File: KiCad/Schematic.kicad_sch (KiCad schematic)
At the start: 44 parts, among them U4 LMH6609MF, U5 LMH6609MF, U6 LMH6609MF, U7 LMH6609MF, U8 LMH6609MF, U9 LMH6609MF

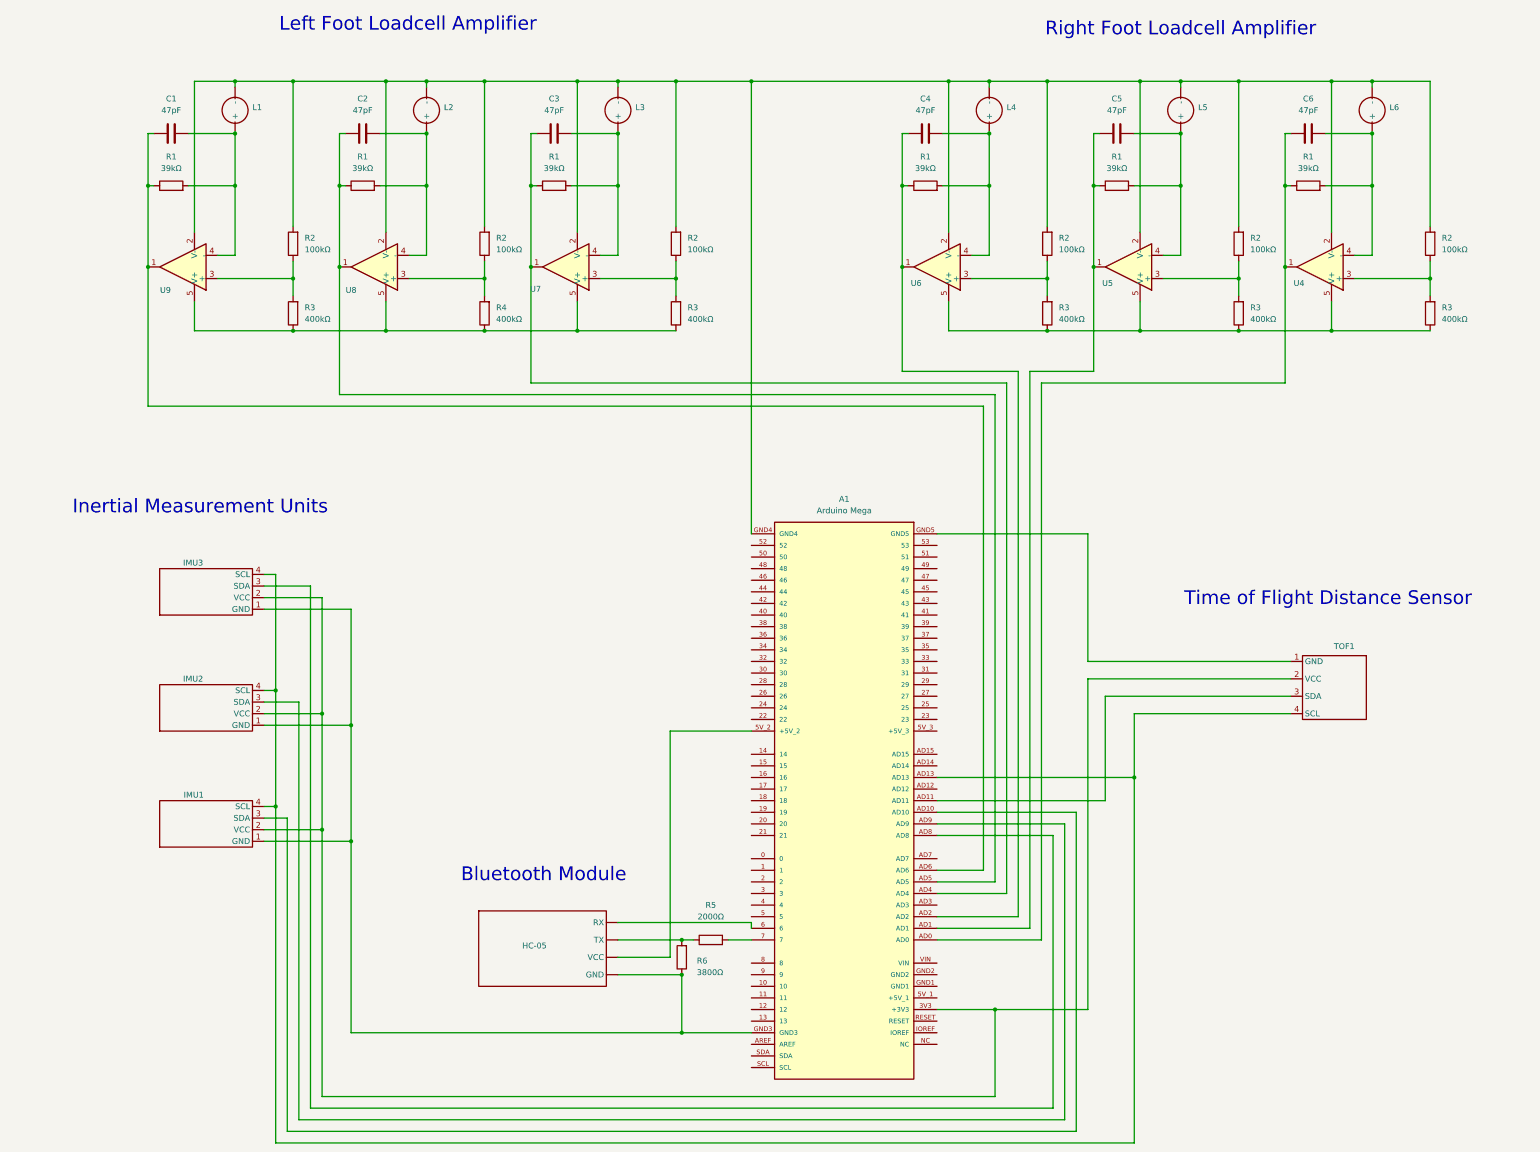
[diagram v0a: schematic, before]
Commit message: Changed wires and Component background color
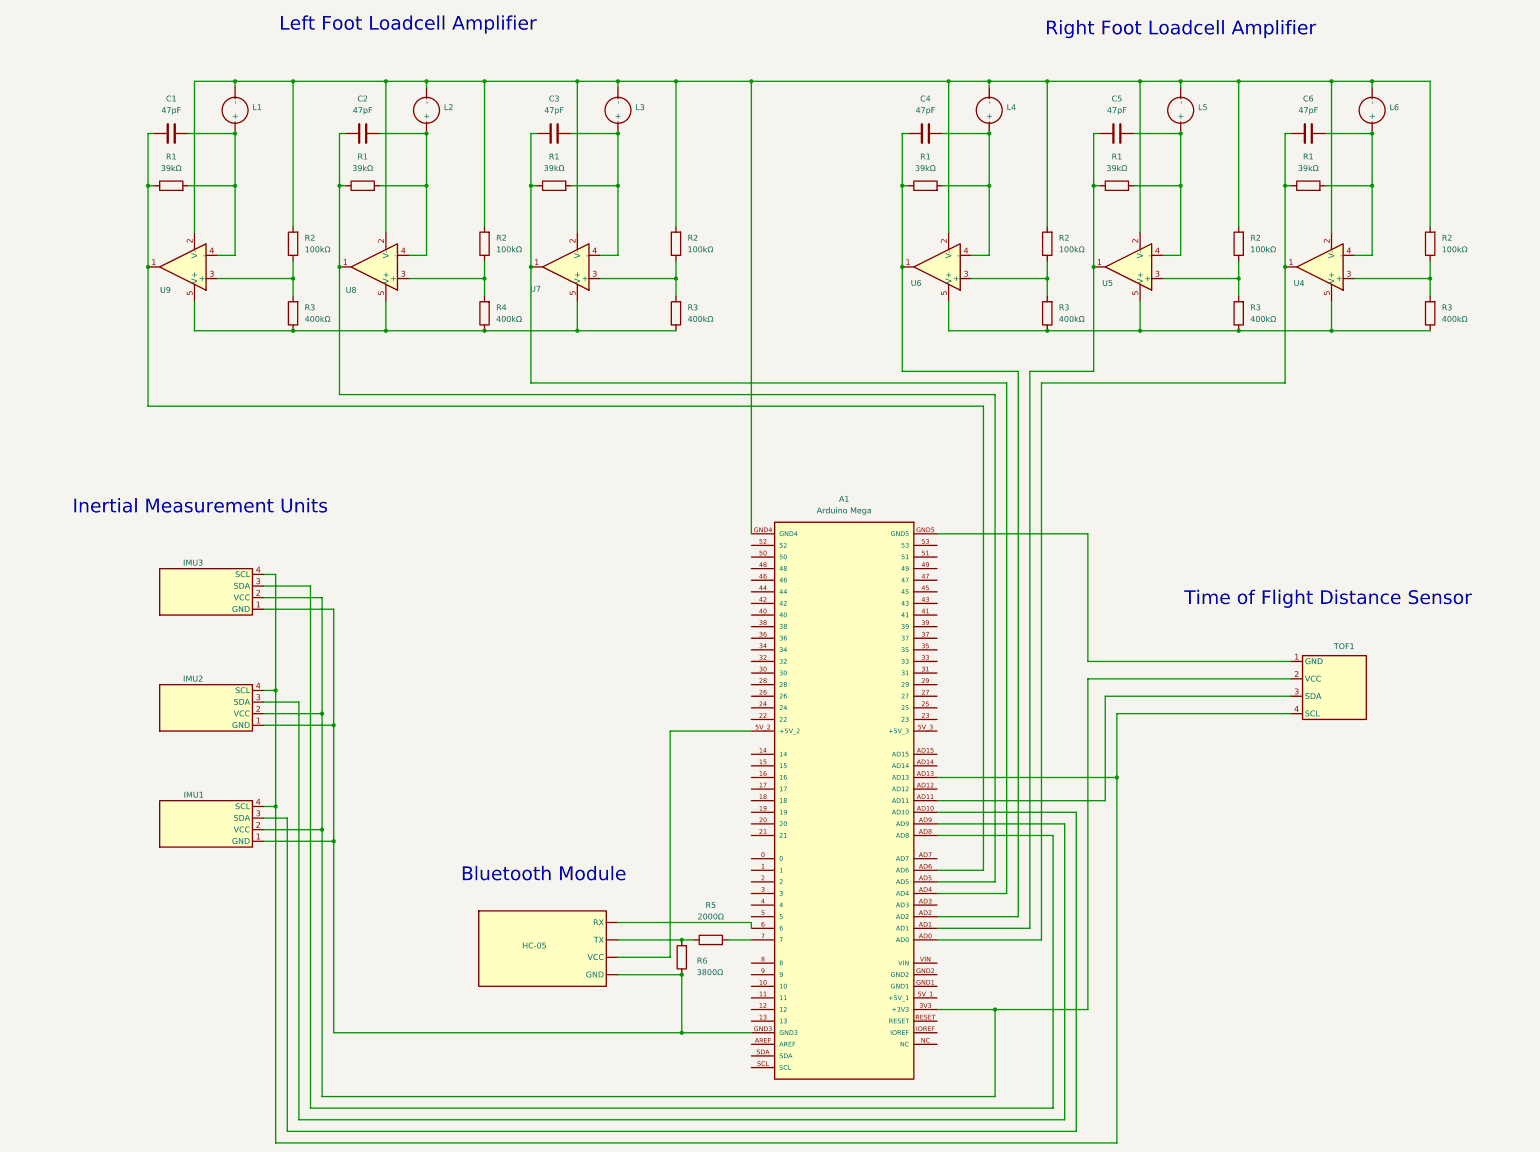
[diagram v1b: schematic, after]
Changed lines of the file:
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@@
 	)
 	(junction
-		(at 113.03 179.07)
-		(diameter 0)
-		(color 0 0 0 0)
-	)
-	(junction
 		(at 185.42 226.06)
 		(diameter 0)
@@
 	)
 	(junction
+		(at 280.67 190.5)
+		(diameter 0)
+		(color 0 0 0 0)
+	)
+	(junction
 		(at 285.75 92.71)
 		(diameter 0)
@@
 	)
 	(junction
-		(at 284.48 190.5)
-		(diameter 0)
-		(color 0 0 0 0)
-	)
-	(junction
 		(at 184.15 81.28)
 		(diameter 0)
@@
 	)
 	(junction
-		(at 113.03 204.47)
-		(diameter 0)
-		(color 0 0 0 0)
-	)
-	(junction
 		(at 120.65 38.1)
 		(diameter 0)
@@
 	)
 	(junction
+		(at 109.22 179.07)
+		(diameter 0)
+		(color 0 0 0 0)
+	)
+	(junction
+		(at 109.22 204.47)
+		(diameter 0)
+		(color 0 0 0 0)
+	)
+	(junction
 		(at 68.58 78.74)
 		(diameter 0)
@@
 	(wire
 		(pts
-			(xy 284.48 176.53) (xy 318.77 176.53)
+			(xy 280.67 176.53) (xy 318.77 176.53)
 		)
 		(stroke
@@
 	(wire
 		(pts
-			(xy 113.03 204.47) (xy 113.03 246.38)
+			(xy 109.22 204.47) (xy 109.22 246.38)
 		)
 		(stroke
@@
 	(wire
 		(pts
-			(xy 96.52 270.51) (xy 284.48 270.51)
+			(xy 96.52 270.51) (xy 280.67 270.51)
 		)
 		(stroke
@@
 	(wire
 		(pts
-			(xy 284.48 190.5) (xy 284.48 176.53)
+			(xy 280.67 190.5) (xy 280.67 176.53)
 		)
 		(stroke
@@
 	(wire
 		(pts
-			(xy 113.03 153.67) (xy 113.03 179.07)
+			(xy 109.22 153.67) (xy 109.22 179.07)
 		)
 		(stroke
@@
 	(wire
 		(pts
-			(xy 93.98 153.67) (xy 113.03 153.67)
+			(xy 93.98 153.67) (xy 109.22 153.67)
 		)
 		(stroke
@@
 	(wire
 		(pts
-			(xy 241.3 190.5) (xy 284.48 190.5)
+			(xy 241.3 190.5) (xy 280.67 190.5)
 		)
 		(stroke
@@
 	(wire
 		(pts
-			(xy 284.48 270.51) (xy 284.48 190.5)
+			(xy 280.67 270.51) (xy 280.67 190.5)
 		)
 		(stroke
@@
 	(wire
 		(pts
-			(xy 113.03 246.38) (xy 185.42 246.38)
+			(xy 109.22 246.38) (xy 185.42 246.38)
 		)
 		(stroke
@@
 	(wire
 		(pts
-			(xy 93.98 204.47) (xy 113.03 204.47)
+			(xy 93.98 204.47) (xy 109.22 204.47)
 		)
 		(stroke
@@
 	(wire
 		(pts
-			(xy 93.98 179.07) (xy 113.03 179.07)
+			(xy 93.98 179.07) (xy 109.22 179.07)
 		)
 		(stroke
@@
 	(wire
 		(pts
-			(xy 113.03 179.07) (xy 113.03 204.47)
+			(xy 109.22 179.07) (xy 109.22 204.47)
 		)
 		(stroke
@@
 	)
 	(symbol
-		(lib_name "Bluetooth_Module_HC-05_1")
 		(lib_id "ProjectSymbols:Bluetooth_Module_HC-05")
 		(at 153.67 228.6 90)

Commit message: Update Schematic.kicad_sch
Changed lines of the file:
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@@
-	)
-	(junction
-		(at 280.67 190.5)
-		(diameter 0)
-		(color 0 0 0 0)
 	)
 	(junction
@@
 	)
 	(junction
+		(at 279.4 190.5)
+		(diameter 0)
+		(color 0 0 0 0)
+	)
+	(junction
 		(at 120.65 92.71)
 		(diameter 0)
@@
 	(wire
 		(pts
-			(xy 280.67 176.53) (xy 318.77 176.53)
+			(xy 279.4 176.53) (xy 318.77 176.53)
 		)
 		(stroke
@@
 	(wire
 		(pts
-			(xy 318.77 172.72) (xy 278.13 172.72)
-		)
-		(stroke
-			(width 0)
-			(type default)
-		)
-	)
-	(wire
-		(pts
-			(xy 96.52 270.51) (xy 280.67 270.51)
+			(xy 318.77 172.72) (xy 276.86 172.72)
+		)
+		(stroke
+			(width 0)
+			(type default)
+		)
+	)
+	(wire
+		(pts
+			(xy 96.52 270.51) (xy 279.4 270.51)
 		)
 		(stroke
@@
 	(wire
 		(pts
-			(xy 280.67 190.5) (xy 280.67 176.53)
+			(xy 279.4 190.5) (xy 279.4 176.53)
 		)
 		(stroke
@@
 	(wire
 		(pts
-			(xy 278.13 195.58) (xy 241.3 195.58)
+			(xy 276.86 195.58) (xy 241.3 195.58)
 		)
 		(stroke
@@
 	(wire
 		(pts
-			(xy 241.3 190.5) (xy 280.67 190.5)
+			(xy 241.3 190.5) (xy 279.4 190.5)
 		)
 		(stroke
@@
 	(wire
 		(pts
-			(xy 278.13 172.72) (xy 278.13 195.58)
-		)
-		(stroke
-			(width 0)
-			(type default)
-		)
-	)
-	(wire
-		(pts
-			(xy 280.67 270.51) (xy 280.67 190.5)
-		)
-		(stroke
+			(xy 276.86 172.72) (xy 276.86 195.58)
+		)
+		(stroke
+			(width 0)
+			(type default)
+		)
+	)
+	(wire
+		(pts
+			(xy 279.4 270.51) (xy 279.4 190.5)
+		)
+		(stroke

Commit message: Added Arduino mega label
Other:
- note added: "Arduino Mega"
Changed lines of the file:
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@@
+		)
+	)
+	(text "Arduino Mega"
+		(exclude_from_sim no)
+		(at 219.964 122.682 0)
+		(effects
+			(font
+				(size 3 3)
+			)
 		)
 	)

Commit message: Schematic update
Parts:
- renumbered IMU3 to IMU1, IMU1 to IMU3, R6 to R10, R5 to R11, R1 to R12, R2 to R13, R3 to R14, R1 to R15, R2 to R16, R3 to R17, R1 to R18, R2 to R19, R3 to R20, R1 to R4, R2 to R5, R4 to R6, R1 to R7, R2 to R8, R3 to R9, U9 to U1, U8 to U2, U7 to U3, U6 to U4, U4 to U6
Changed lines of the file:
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@@
 			(font
 				(size 3 3)
+				(thickness 0.6)
+				(bold yes)
 			)
 		)
@@
 	(text "Arduino Mega"
 		(exclude_from_sim no)
-		(at 219.964 122.682 0)
+		(at 220.472 126.746 0)
 		(effects
 			(font
 				(size 3 3)
+				(thickness 0.6)
+				(bold yes)
 			)
 		)
@@
 	(text "Bluetooth Module"
 		(exclude_from_sim no)
-		(at 155.194 211.836 0)
+		(at 156.464 213.36 0)
 		(effects
 			(font
 				(size 3 3)
+				(thickness 0.6)
+				(bold yes)
 			)
 		)
@@
 	(text "Inertial Measurement Units"
 		(exclude_from_sim no)
-		(at 80.01 131.318 0)
+		(at 77.47 134.874 0)
 		(effects
 			(font
 				(size 3 3)
+				(thickness 0.6)
+				(bold yes)
 			)
 		)
@@
 			(font
 				(size 3 3)
+				(thickness 0.6)
+				(bold yes)
 			)
 		)
@@
 			(font
 				(size 3 3)
+				(thickness 0.6)
+				(bold yes)
 			)
 		)
@@
 		(on_board yes)
 		(dnp no)
-		(property "Reference" "U4"
-			(at 320.548 82.296 0)
+		(property "Reference" "U6"
+			(at 320.548 74.168 0)
 			(effects
 				(font
@@
 			(project "Schematic"
 				(path "/8a716230-69e7-45b9-8b64-edac5da98bb8"
-					(reference "U4")
+					(reference "U6")
 					(unit 1)
 				)
@@
 		(dnp no)
 		(fields_autoplaced yes)
-		(property "Reference" "R2"
+		(property "Reference" "R16"
 			(at 309.88 72.3899 0)
 			(effects
@@
 			(project "Schematic"
 				(path "/8a716230-69e7-45b9-8b64-edac5da98bb8"
-					(reference "R2")
+					(reference "R16")
 					(unit 1)
 				)
@@
 		(dnp no)
 		(fields_autoplaced yes)
-		(property "Reference" "R3"
+		(property "Reference" "R17"
 			(at 309.88 87.6299 0)
 			(effects
@@
 			(project "Schematic"
 				(path "/8a716230-69e7-45b9-8b64-edac5da98bb8"
-					(reference "R3")
+					(reference "R17")
 					(unit 1)
 				)
@@
 		(dnp no)
 		(fields_autoplaced yes)
-		(property "Reference" "R3"
+		(property "Reference" "R9"
 			(at 186.69 87.6299 0)
 			(effects
@@
 			(project "Schematic"
 				(path "/8a716230-69e7-45b9-8b64-edac5da98bb8"
-					(reference "R3")
+					(reference "R9")
 					(unit 1)
 				)
@@
 		(on_board yes)
 		(dnp no)
-		(property "Reference" "U6"
-			(at 236.728 82.296 0)
+		(property "Reference" "U4"
+			(at 236.728 74.168 0)
 			(effects
 				(font
@@
 			(project "Schematic"
 				(path "/8a716230-69e7-45b9-8b64-edac5da98bb8"
-					(reference "U6")
+					(reference "U4")
 					(unit 1)
 				)
@@
 		(on_board yes)
 		(dnp no)
-		(property "Reference" "U7"
-			(at 153.416 83.566 0)
+		(property "Reference" "U3"
+			(at 155.956 74.168 0)
 			(effects
 				(font
@@
 			(project "Schematic"
 				(path "/8a716230-69e7-45b9-8b64-edac5da98bb8"
-					(reference "U7")
+					(reference "U3")
 					(unit 1)
 				)
@@
 		(dnp no)
 		(fields_autoplaced yes)
-		(property "Reference" "R2"
+		(property "Reference" "R19"
 			(at 351.79 72.3899 0)
 			(effects
@@
 			(project "Schematic"
 				(path "/8a716230-69e7-45b9-8b64-edac5da98bb8"
-					(reference "R2")
+					(reference "R19")
 					(unit 1)
 				)
@@
 		(dnp no)
 		(fields_autoplaced yes)
-		(property "Reference" "R1"
+		(property "Reference" "R15"
 			(at 280.67 54.61 90)
 			(effects
@@
 			(project "Schematic"
 				(path "/8a716230-69e7-45b9-8b64-edac5da98bb8"
-					(reference "R1")
+					(reference "R15")
 					(unit 1)
 				)
@@
 		(dnp no)
 		(property "Reference" "IMU2"
-			(at 80.6449 168.91 90)
+			(at 81.534 173.99 90)
 			(effects
 				(font
@@
 		(dnp no)
 		(fields_autoplaced yes)
-		(property "Reference" "R1"
+		(property "Reference" "R4"
 			(at 115.57 54.61 90)
 			(effects
@@
 			(project "Schematic"
 				(path "/8a716230-69e7-45b9-8b64-edac5da98bb8"
-					(reference "R1")
+					(reference "R4")
 					(unit 1)
 				)
@@
 		(on_board yes)
 		(dnp no)
-		(property "Reference" "R5"
+		(property "Reference" "R11"
 			(at 191.77 218.44 90)
 			(effects
@@
 			(project "Schematic"
 				(path "/8a716230-69e7-45b9-8b64-edac5da98bb8"
-					(reference "R5")
+					(reference "R11")
 					(unit 1)
 				)
@@
 		(dnp no)
 		(fields_autoplaced yes)
-		(property "Reference" "R1"
+		(property "Reference" "R12"
 			(at 238.76 54.61 90)
 			(effects
@@
 			(project "Schematic"
 				(path "/8a716230-69e7-45b9-8b64-edac5da98bb8"
-					(reference "R1")
+					(reference "R12")
 					(unit 1)
 				)
@@
 		(on_board yes)
 		(dnp no)
-		(fields_autoplaced yes)
 		(property "Reference" "A1"
-			(at 220.98 129.54 0)
+			(at 221.234 132.588 0)
 			(effects
 				(font
@@
 					(size 1.27 1.27)
 				)
+				(hide yes)
 			)
 		)
@@
 		(on_board yes)
 		(dnp no)
-		(property "Reference" "U9"
-			(at 72.39 83.82 0)
+		(property "Reference" "U1"
+			(at 71.882 74.422 0)
 			(effects
 				(font
@@
 			(project "Schematic"
 				(path "/8a716230-69e7-45b9-8b64-edac5da98bb8"
-					(reference "U9")
+					(reference "U1")
 					(unit 1)
 				)
@@
 		(dnp no)
 		(fields_autoplaced yes)
-		(property "Reference" "R3"
+		(property "Reference" "R20"
 			(at 351.79 87.6299 0)
 			(effects
@@
 			(project "Schematic"
 				(path "/8a716230-69e7-45b9-8b64-edac5da98bb8"
-					(reference "R3")
+					(reference "R20")
 					(unit 1)
 				)
@@
 		(dnp no)
 		(property "Reference" "U5"
-			(at 278.638 82.296 0)
+			(at 278.638 74.168 0)
 			(effects
 				(font
@@
 		(on_board yes)
 		(dnp no)
-		(property "Reference" "R6"
+		(property "Reference" "R10"
 			(at 188.722 230.632 0)
 			(effects
@@
 			(project "Schematic"
 				(path "/8a716230-69e7-45b9-8b64-edac5da98bb8"
-					(reference "R6")
+					(reference "R10")
 					(unit 1)
 				)
@@
 		(on_board yes)
 		(dnp no)
-		(property "Reference" "IMU1"
-			(at 80.772 194.31 90)
+		(property "Reference" "IMU3"
+			(at 81.6611 199.39 90)
 			(effects
 				(font
@@
 			(project ""
 				(path "/8a716230-69e7-45b9-8b64-edac5da98bb8"
-					(reference "IMU1")
+					(reference "IMU3")
 					(unit 1)
 				)
@@
 		(dnp no)
 		(fields_autoplaced yes)
-		(property "Reference" "R2"
+		(property "Reference" "R13"
 			(at 267.97 72.3899 0)
 			(effects
@@
 			(project "Schematic"
 				(path "/8a716230-69e7-45b9-8b64-edac5da98bb8"
-					(reference "R2")
+					(reference "R13")
 					(unit 1)
 				)
@@
 		(dnp no)
 		(fields_autoplaced yes)
-		(property "Reference" "R3"
+		(property "Reference" "R14"
 			(at 267.97 87.6299 0)
 			(effects
@@
 			(project "Schematic"
 				(path "/8a716230-69e7-45b9-8b64-edac5da98bb8"
-					(reference "R3")
+					(reference "R14")
 					(unit 1)
 				)
@@
 		(dnp no)
 		(fields_autoplaced yes)
-		(property "Reference" "R2"
+		(property "Reference" "R5"
 			(at 144.78 72.3899 0)
 			(effects
@@
 			(project "Schematic"
 				(path "/8a716230-69e7-45b9-8b64-edac5da98bb8"
-					(reference "R2")
+					(reference "R5")
 					(unit 1)
 				)
@@
 		(on_board yes)
 		(dnp no)
-		(property "Reference" "IMU3"
-			(at 80.6449 143.51 90)
+		(property "Reference" "IMU1"
+			(at 81.534 148.59 90)
 			(effects
 				(font
@@
 			(project "Schematic"
 				(path "/8a716230-69e7-45b9-8b64-edac5da98bb8"
-					(reference "IMU3")
+					(reference "IMU1")
 					(unit 1)
 				)
@@
 		(dnp no)
 		(fields_autoplaced yes)
-		(property "Reference" "R1"
+		(property "Reference" "R18"
 			(at 322.58 54.61 90)
 			(effects
@@
 			(project "Schematic"
 				(path "/8a716230-69e7-45b9-8b64-edac5da98bb8"
-					(reference "R1")
+					(reference "R18")
 					(unit 1)
 				)
@@
 		(dnp no)
 		(fields_autoplaced yes)
-		(property "Reference" "R2"
+		(property "Reference" "R8"
 			(at 186.69 72.3899 0)
 			(effects
@@
 			(project "Schematic"
 				(path "/8a716230-69e7-45b9-8b64-edac5da98bb8"
-					(reference "R2")
+					(reference "R8")
 					(unit 1)
 				)
@@
 		(on_board yes)
 		(dnp no)
-		(property "Reference" "U8"
-			(at 113.03 83.82 0)
+		(property "Reference" "U2"
+			(at 112.776 74.676 0)
 			(effects
 				(font
@@
 			(project "Schematic"
 				(path "/8a716230-69e7-45b9-8b64-edac5da98bb8"
-					(reference "U8")
+					(reference "U2")
 					(unit 1)
 				)
@@
 		(dnp no)
 		(fields_autoplaced yes)
-		(property "Reference" "R4"
+		(property "Reference" "R6"
 			(at 144.78 87.6299 0)
 			(effects
@@
 			(project "Schematic"
 				(path "/8a716230-69e7-45b9-8b64-edac5da98bb8"
-					(reference "R4")
+					(reference "R6")
 					(unit 1)
 				)
@@
 		(dnp no)
 		(property "Reference" "TOF1"
-			(at 328.168 161.798 90)
+			(at 329.184 170.688 90)
 			(effects
 				(font
@@
 		(dnp no)
 		(fields_autoplaced yes)
-		(property "Reference" "R1"
+		(property "Reference" "R7"
 			(at 157.48 54.61 90)
 			(effects
@@
 			(project "Schematic"
 				(path "/8a716230-69e7-45b9-8b64-edac5da98bb8"
-					(reference "R1")
+					(reference "R7")
 					(unit 1)
 				)
